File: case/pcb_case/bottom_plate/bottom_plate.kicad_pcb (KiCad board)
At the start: 2 copper layers, 143.4 x 111.8 mm, 2 parts

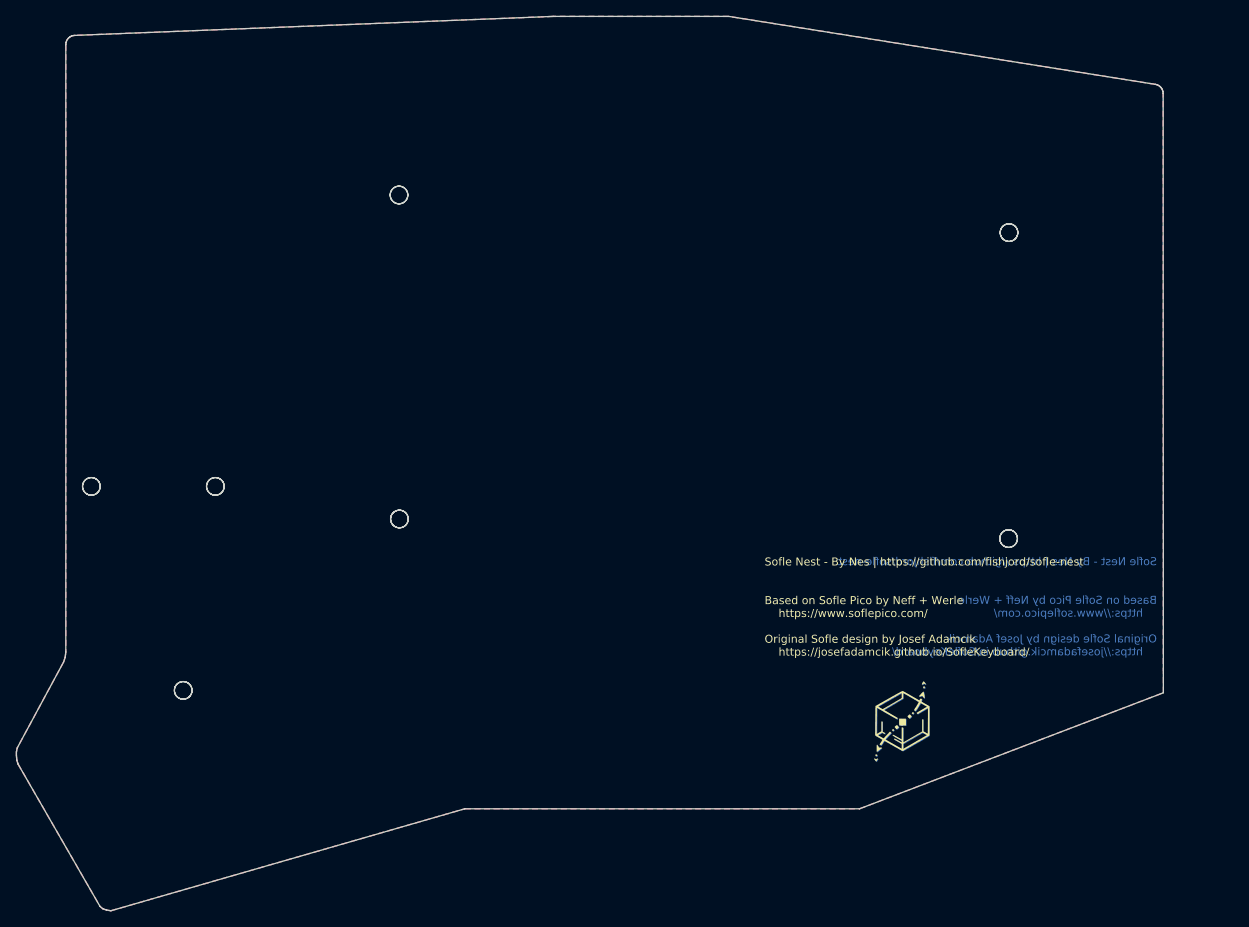
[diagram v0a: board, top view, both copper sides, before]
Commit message: Fix issues with case plates found during fabrication eval.
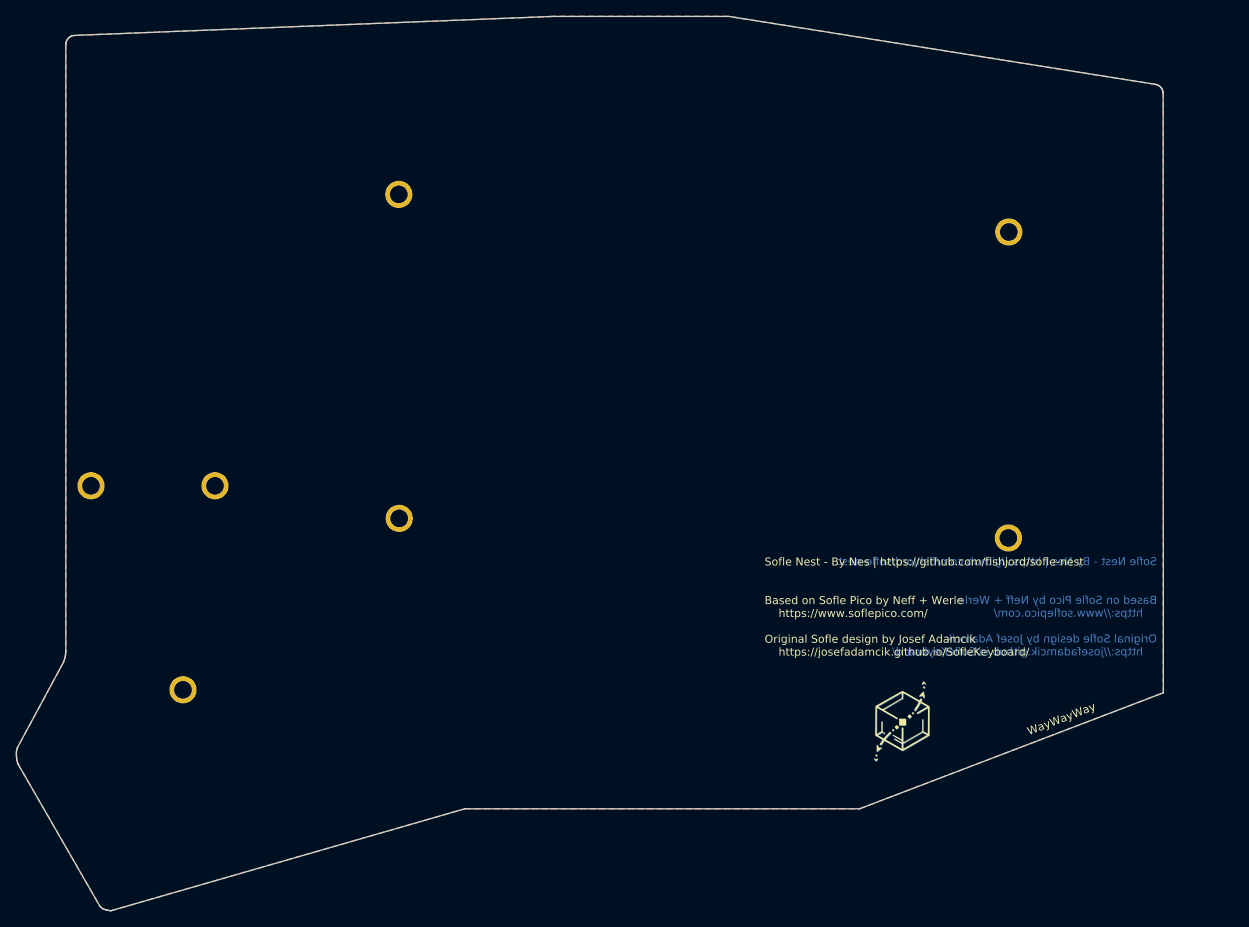
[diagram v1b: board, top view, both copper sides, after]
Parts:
- added TH1: HOLE, Sofle_Nest:backplate_hole_M2_terminate, F.Cu at (91.5, 93.7)
- added TH2: HOLE, Sofle_Nest:backplate_hole_M2_terminate, F.Cu at (107.0, 93.7)
- added TH3: HOLE, Sofle_Nest:backplate_hole_M2_terminate, F.Cu at (130.0, 57.3)
- added TH4: HOLE, Sofle_Nest:backplate_hole_M2_terminate, F.Cu at (206.2, 62.0)
- added TH5: HOLE, Sofle_Nest:backplate_hole_M2_terminate, F.Cu at (206.2, 100.2)
- added TH6: HOLE, Sofle_Nest:backplate_hole_M2_terminate, F.Cu at (130.0, 97.8)
- added TH7: HOLE, Sofle_Nest:backplate_hole_M2_terminate, F.Cu at (103.0, 119.2)
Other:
- outline, holes or cut-outs redrawn
- board text added: "JLCJLCJLCJLC"
- board text added: "WayWayWay"
